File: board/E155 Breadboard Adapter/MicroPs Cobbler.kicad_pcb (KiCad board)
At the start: 2 copper layers, 61 x 66.4 mm, 3 parts, among them J1 Conn_01x20, J2 40-pin Ribbon Cable Connector, J3 Conn_01x20

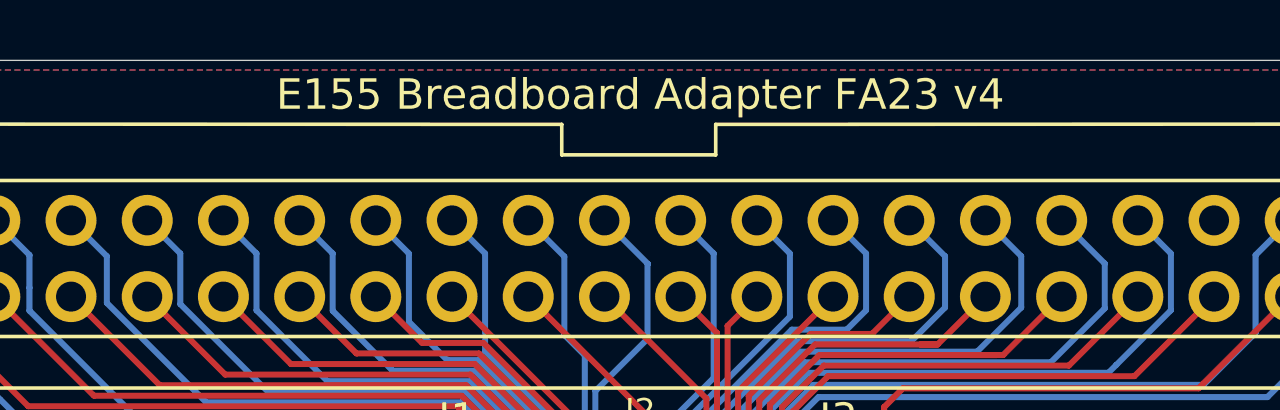
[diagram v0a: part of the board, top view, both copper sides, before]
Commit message: Board updates for FA24
Removed specific text on the board which references a year and changed it to a version number. Also updated the libraries and KiCad files to resolve design check issues.
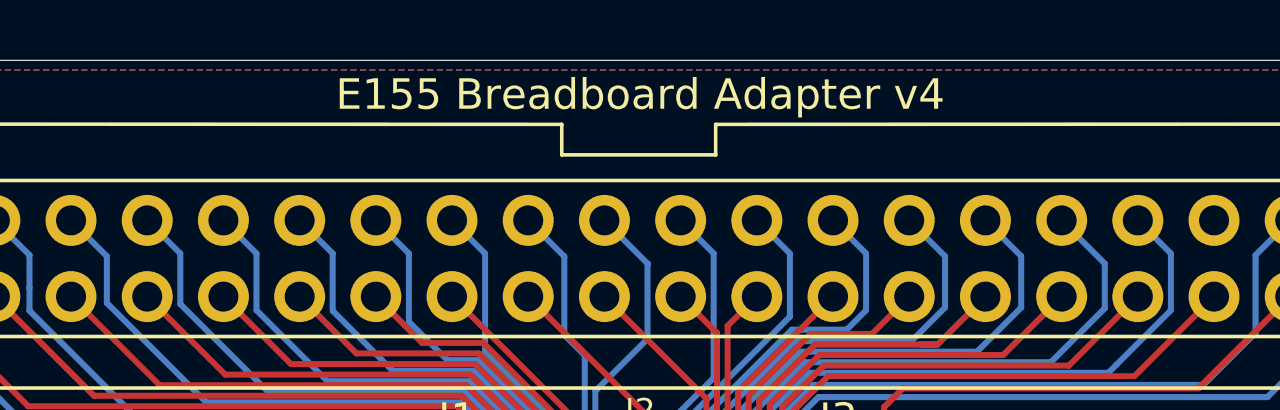
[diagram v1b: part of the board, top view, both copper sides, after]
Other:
- board text added: "E155 Breadboard Adapter v4"
- board text removed: "E155 Breadboard Adapter FA23 v4"
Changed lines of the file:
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@@
     (effects (font (size 1 1) (thickness 0.1)))
   )
-  (gr_text "E155 Breadboard Adapter FA23 v4" (at 153.416 56.388) (layer "F.SilkS")
+  (gr_text "E155 Breadboard Adapter v4" (at 153.416 56.388) (layer "F.SilkS")
     (effects (font (size 1.016 1.016) (thickness 0.127)))
   )
